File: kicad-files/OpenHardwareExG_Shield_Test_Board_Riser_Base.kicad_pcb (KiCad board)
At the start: 4 copper layers, 147.3 x 81.3 mm, 12 parts

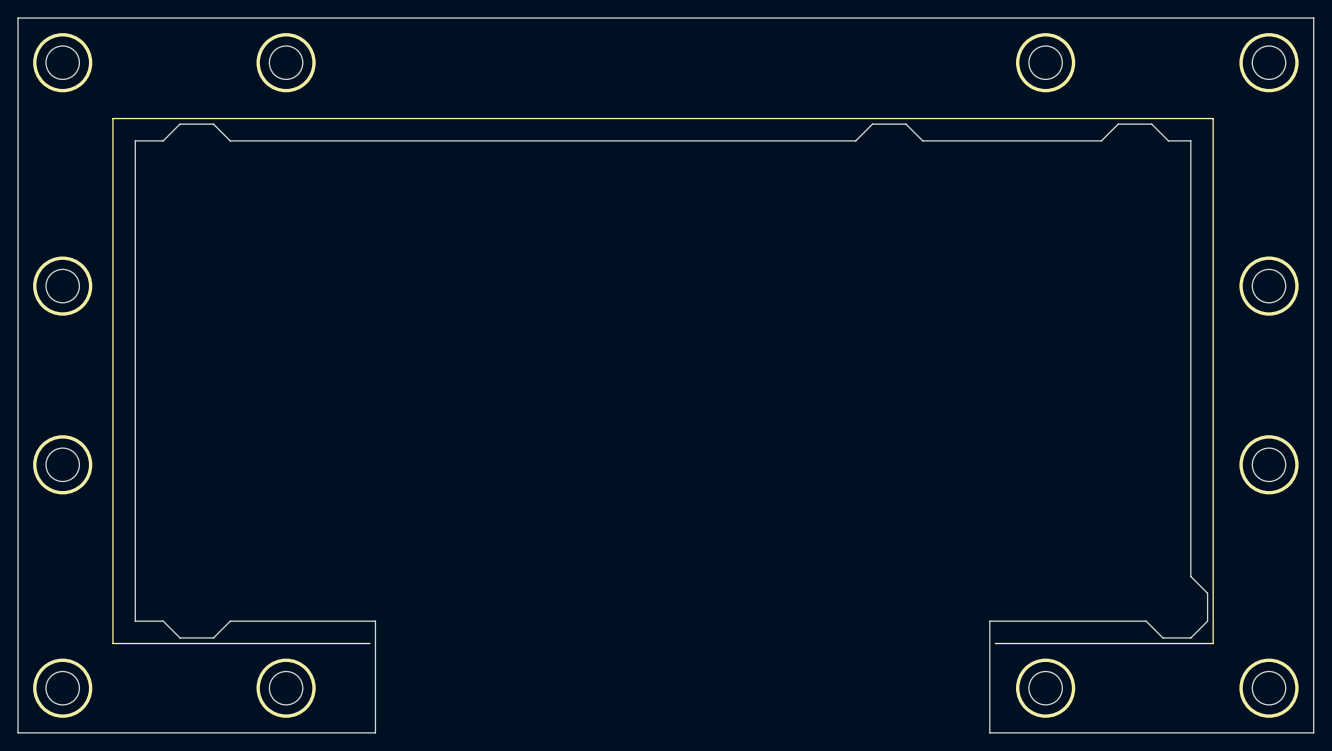
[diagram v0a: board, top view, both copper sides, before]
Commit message: expand test jig board to stabilize pogo pins
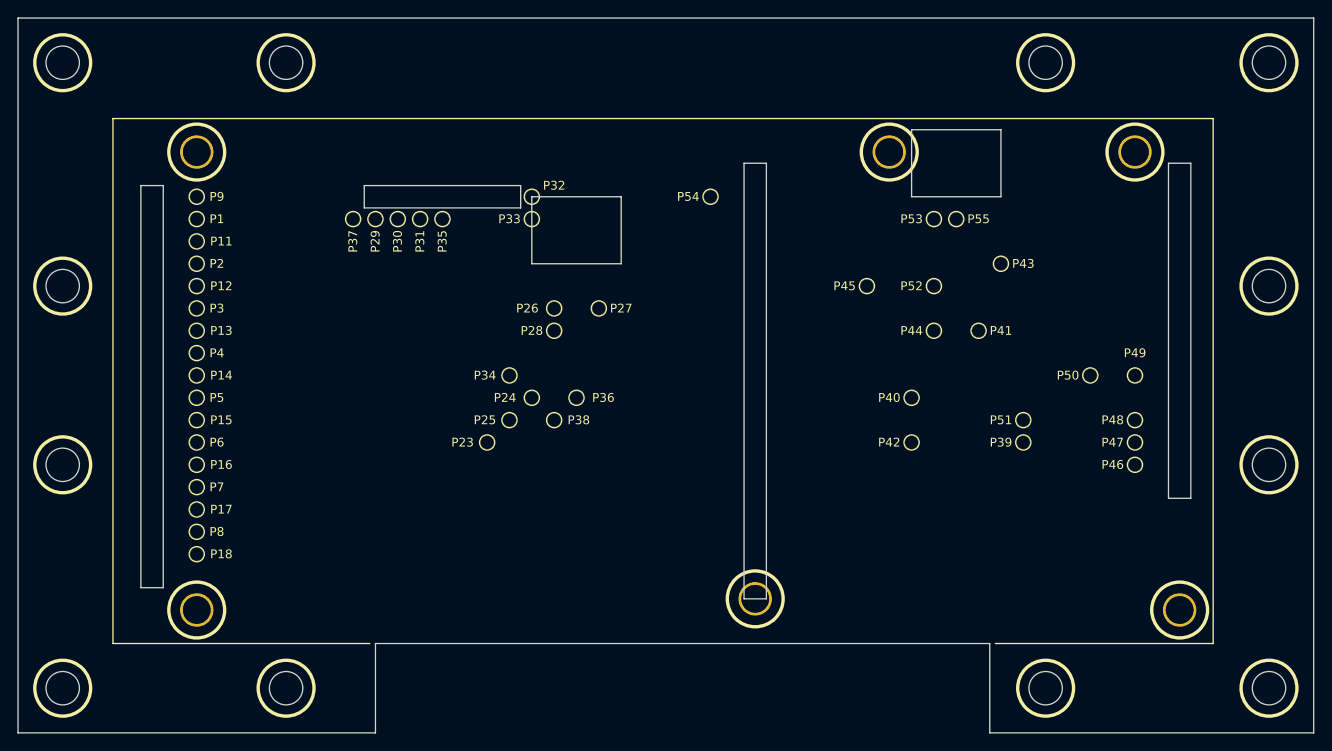
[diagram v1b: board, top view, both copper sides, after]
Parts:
- added Hole_M3: VAL**, Hole_M3, F.Cu at (180.3, 85.1)
- added Hole_M3: VAL**, Hole_M3, F.Cu at (132.1, 83.8)
- added Hole_M3: VAL**, Hole_M3, F.Cu at (175.3, 33.0)
- added Hole_M3: VAL**, Hole_M3, F.Cu at (147.3, 33.0)
- added Hole_M3: VAL**, Hole_M3, F.Cu at (68.6, 33.0)
- added Hole_M3: VAL**, Hole_M3, F.Cu at (68.6, 85.1)
- added P1: CONN_1, connectors:POGO_HEAD_HOLE, F.Cu at (68.6, 40.6)
- added P11: CONN_1, connectors:POGO_HEAD_HOLE, F.Cu at (68.6, 43.2)
- added P12: CONN_1, connectors:POGO_HEAD_HOLE, F.Cu at (68.6, 48.3)
- added P13: CONN_1, connectors:POGO_HEAD_HOLE, F.Cu at (68.6, 53.3)
- added P14: CONN_1, connectors:POGO_HEAD_HOLE, F.Cu at (68.6, 58.4)
- added P15: CONN_1, connectors:POGO_HEAD_HOLE, F.Cu at (68.6, 63.5)
- added P16: CONN_1, connectors:POGO_HEAD_HOLE, F.Cu at (68.6, 68.6)
- added P17: CONN_1, connectors:POGO_HEAD_HOLE, F.Cu at (68.6, 73.7)
- added P18: CONN_1, connectors:POGO_HEAD_HOLE, F.Cu at (68.6, 78.7)
- added P2: CONN_1, connectors:POGO_HEAD_HOLE, F.Cu at (68.6, 45.7)
- added P23: CONN_1, connectors:POGO_HEAD_HOLE, F.Cu at (101.6, 66.0)
- added P24: CONN_1, connectors:POGO_HEAD_HOLE, F.Cu at (106.7, 61.0)
- added P25: CONN_1, connectors:POGO_HEAD_HOLE, F.Cu at (104.1, 63.5)
- added P26: CONN_1, connectors:POGO_HEAD_HOLE, F.Cu at (109.2, 50.8)
- added P27: CONN_1, connectors:POGO_HEAD_HOLE, F.Cu at (114.3, 50.8)
- added P28: CONN_1, connectors:POGO_HEAD_HOLE, F.Cu at (109.2, 53.3)
- added P29: CONN_1, connectors:POGO_HEAD_HOLE, F.Cu at (88.9, 40.6)
- added P3: CONN_1, connectors:POGO_HEAD_HOLE, F.Cu at (68.6, 50.8)
- added P30: CONN_1, connectors:POGO_HEAD_HOLE, F.Cu at (91.4, 40.6)
- added P31: CONN_1, connectors:POGO_HEAD_HOLE, F.Cu at (94.0, 40.6)
- added P32: CONN_1, connectors:POGO_HEAD_HOLE, F.Cu at (106.7, 38.1)
- added P33: CONN_1, connectors:POGO_HEAD_HOLE, F.Cu at (106.7, 40.6)
- added P34: CONN_1, connectors:POGO_HEAD_HOLE, F.Cu at (104.1, 58.4)
- added P35: CONN_1, connectors:POGO_HEAD_HOLE, F.Cu at (96.5, 40.6)
- added P36: CONN_1, connectors:POGO_HEAD_HOLE, F.Cu at (111.8, 61.0)
- added P37: CONN_1, connectors:POGO_HEAD_HOLE, F.Cu at (86.4, 40.6)
- added P38: CONN_1, connectors:POGO_HEAD_HOLE, F.Cu at (109.2, 63.5)
- added P39: CONN_1, connectors:POGO_HEAD_HOLE, F.Cu at (162.6, 66.0)
- added P4: CONN_1, connectors:POGO_HEAD_HOLE, F.Cu at (68.6, 55.9)
- added P40: CONN_1, connectors:POGO_HEAD_HOLE, F.Cu at (149.9, 61.0)
- added P41: CONN_1, connectors:POGO_HEAD_HOLE, F.Cu at (157.5, 53.3)
- added P42: CONN_1, connectors:POGO_HEAD_HOLE, F.Cu at (149.9, 66.0)
- added P43: CONN_1, connectors:POGO_HEAD_HOLE, F.Cu at (160.0, 45.7)
- added P44: CONN_1, connectors:POGO_HEAD_HOLE, F.Cu at (152.4, 53.3)
- added P45: CONN_1, connectors:POGO_HEAD_HOLE, F.Cu at (144.8, 48.3)
- added P46: CONN_1, connectors:POGO_HEAD_HOLE, F.Cu at (175.3, 68.6)
- added P47: CONN_1, connectors:POGO_HEAD_HOLE, F.Cu at (175.3, 66.0)
- added P48: CONN_1, connectors:POGO_HEAD_HOLE, F.Cu at (175.3, 63.5)
- added P49: CONN_1, connectors:POGO_HEAD_HOLE, F.Cu at (175.3, 58.4)
- added P5: CONN_1, connectors:POGO_HEAD_HOLE, F.Cu at (68.6, 61.0)
- added P50: CONN_1, connectors:POGO_HEAD_HOLE, F.Cu at (170.2, 58.4)
- added P51: CONN_1, connectors:POGO_HEAD_HOLE, F.Cu at (162.6, 63.5)
- added P52: CONN_1, connectors:POGO_HEAD_HOLE, F.Cu at (152.4, 48.3)
- added P53: CONN_1, connectors:POGO_HEAD_HOLE, F.Cu at (152.4, 40.6)
- added P54: CONN_1, connectors:POGO_HEAD_HOLE, F.Cu at (127.0, 38.1)
- added P55: CONN_1, connectors:POGO_HEAD_HOLE, F.Cu at (154.9, 40.6)
- added P6: CONN_1, connectors:POGO_HEAD_HOLE, F.Cu at (68.6, 66.0)
- added P7: CONN_1, connectors:POGO_HEAD_HOLE, F.Cu at (68.6, 71.1)
- added P8: CONN_1, connectors:POGO_HEAD_HOLE, F.Cu at (68.6, 76.2)
- added P9: CONN_1, connectors:POGO_HEAD_HOLE, F.Cu at (68.6, 38.1)
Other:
- outline, holes or cut-outs redrawn
